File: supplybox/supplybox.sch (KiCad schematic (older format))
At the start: 12 parts, among them J1 Screw_Terminal_01x02

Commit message: v1.0
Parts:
- removed C?: CP, symbol Device:CP
- removed FL1: EMI_Filter_CommonMode, Inductor_THT:L_CommonMode_Wuerth_WE-CMB-XS, symbol Device:EMI_Filter_CommonMode
- removed J1: Screw_Terminal_01x02, symbol Connector:Screw_Terminal_01x02
- added C10, C6: 470uF, Capacitor_THT:CP_Radial_D8.0mm_P3.50mm, symbol Device:CP
- added C11, C4, C7, C8: 100uF, Capacitor_THT:CP_Radial_D6.3mm_P2.50mm, symbol Device:CP
- added C2: 100nF, Capacitor_SMD:C_0603_1608Metric_Pad1.05x0.95mm_HandSolder, symbol Device:C
- added C5, C9: 470pF, Capacitor_SMD:C_0603_1608Metric_Pad1.05x0.95mm_HandSolder, symbol Device:C
- added D4, D5: 1N5819, Diode_THT:D_DO-41_SOD81_P10.16mm_Horizontal, symbol Diode:1N5819
- added FL1: L_Core_Ferrite_Coupled_1243, Inductor_THT:L_CommonMode_Wuerth_WE-CMB-XS, symbol Device:L_Core_Ferrite_Coupled_1243
- added H1, H2, H3, H4, H5, H6, H7, H8: MountingHole_Pad, MountingHole:MountingHole_3.2mm_M3_DIN965_Pad, symbol Mechanical:MountingHole_Pad
- added L1, L3: 220 uH, Inductor_THT:L_Radial_D9.5mm_P5.00mm_Fastron_07HVP, symbol Device:L_Core_Ferrite
- added L2, L4: 1uH, Inductor_SMD:L_0805_2012Metric_Pad1.15x1.40mm_HandSolder, symbol Device:L_Core_Ferrite
- added R2, R5: 0.3 Ohm, Resistor_SMD:R_0805_2012Metric_Pad1.15x1.40mm_HandSolder, symbol Device:R
- added R3: 1200, Resistor_SMD:R_0603_1608Metric_Pad1.05x0.95mm_HandSolder, symbol Device:R
- added R4, R7: 3900, Resistor_SMD:R_0603_1608Metric_Pad1.05x0.95mm_HandSolder, symbol Device:R
- added R6: 2200, Resistor_SMD:R_0603_1608Metric_Pad1.05x0.95mm_HandSolder, symbol Device:R
- added RV1, RV2: 0-200, Potentiometer_SMD:Potentiometer_Bourns_TC33X_Vertical, symbol Device:R_POT_TRIM
- added TH1: Thermistor_NTC, Resistor_THT:R_Axial_DIN0204_L3.6mm_D1.6mm_P5.08mm_Horizontal, symbol Device:Thermistor_NTC
- added TP1, TP10, TP2, TP3, TP4, TP8, TP9: TestPoint, TestPoint:TestPoint_Pad_D1.0mm, symbol Connector:TestPoint
- added U1: EPM1210SJ_1212AE, ERIG_Converter_DCDC:EPMXX10SJ_XXXXAE, symbol ERIG_Converter_DCDC:EPM1210SJ_1212AE
- added U2, U3: MC33063AD, Package_SO:SOIC-8_3.9x4.9mm_P1.27mm, symbol Regulator_Switching:MC33063AD
- C1: value 1000uF -> 100uF; footprint (none) -> Capacitor_THT:CP_Radial_D18.0mm_P7.50mm; digikey (none) -> 565-1481-ND
- C3: renamed from C?; value C -> 47nF; footprint (none) -> Capacitor_SMD:C_0603_1608Metric_Pad1.05x0.95mm_HandSolder; digikey (none) -> 1292-1446-1-ND
- D1: renamed from D?; footprint (none) -> ERIG_Diode:KBP20XXG; digikey (none) -> KBP206GDI-ND
- D2: renamed from D?; value D_Zener 13V -> 13V; footprint (none) -> Diode_SMD:D_SOT-23_ANK; digikey (none) -> BZX84C13LT1GOSCT-ND
- D3: renamed from D?; footprint (none) -> Package_TO_SOT_THT:TO-92; digikey (none) -> 1740-1089-1-ND
- F1, F2: footprint (none) -> ERIG_Fuse:RST_XXX; digikey RST100AMMO-ND -> 507-1166-ND
- F3: footprint (none) -> Fuse:Fuse_0805_2012Metric_Pad1.15x1.40mm_HandSolder; digikey (none) -> MFU08051.00CT-ND
- R1: renamed from R?; value R -> 1K; footprint (none) -> Resistor_SMD:R_0603_1608Metric_Pad1.05x0.95mm_HandSolder; digikey (none) -> RHM1.0KDCT-ND
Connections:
- net labels added: +12V, +3.3V, +5V, 12V_Unfused, DC+L, GND
- wire segments 38 -> 108
- no-connect marks 0 -> 2
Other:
- moved on the sheet: C1, C3, D1, D2, D3, F1, F2, F3, R1

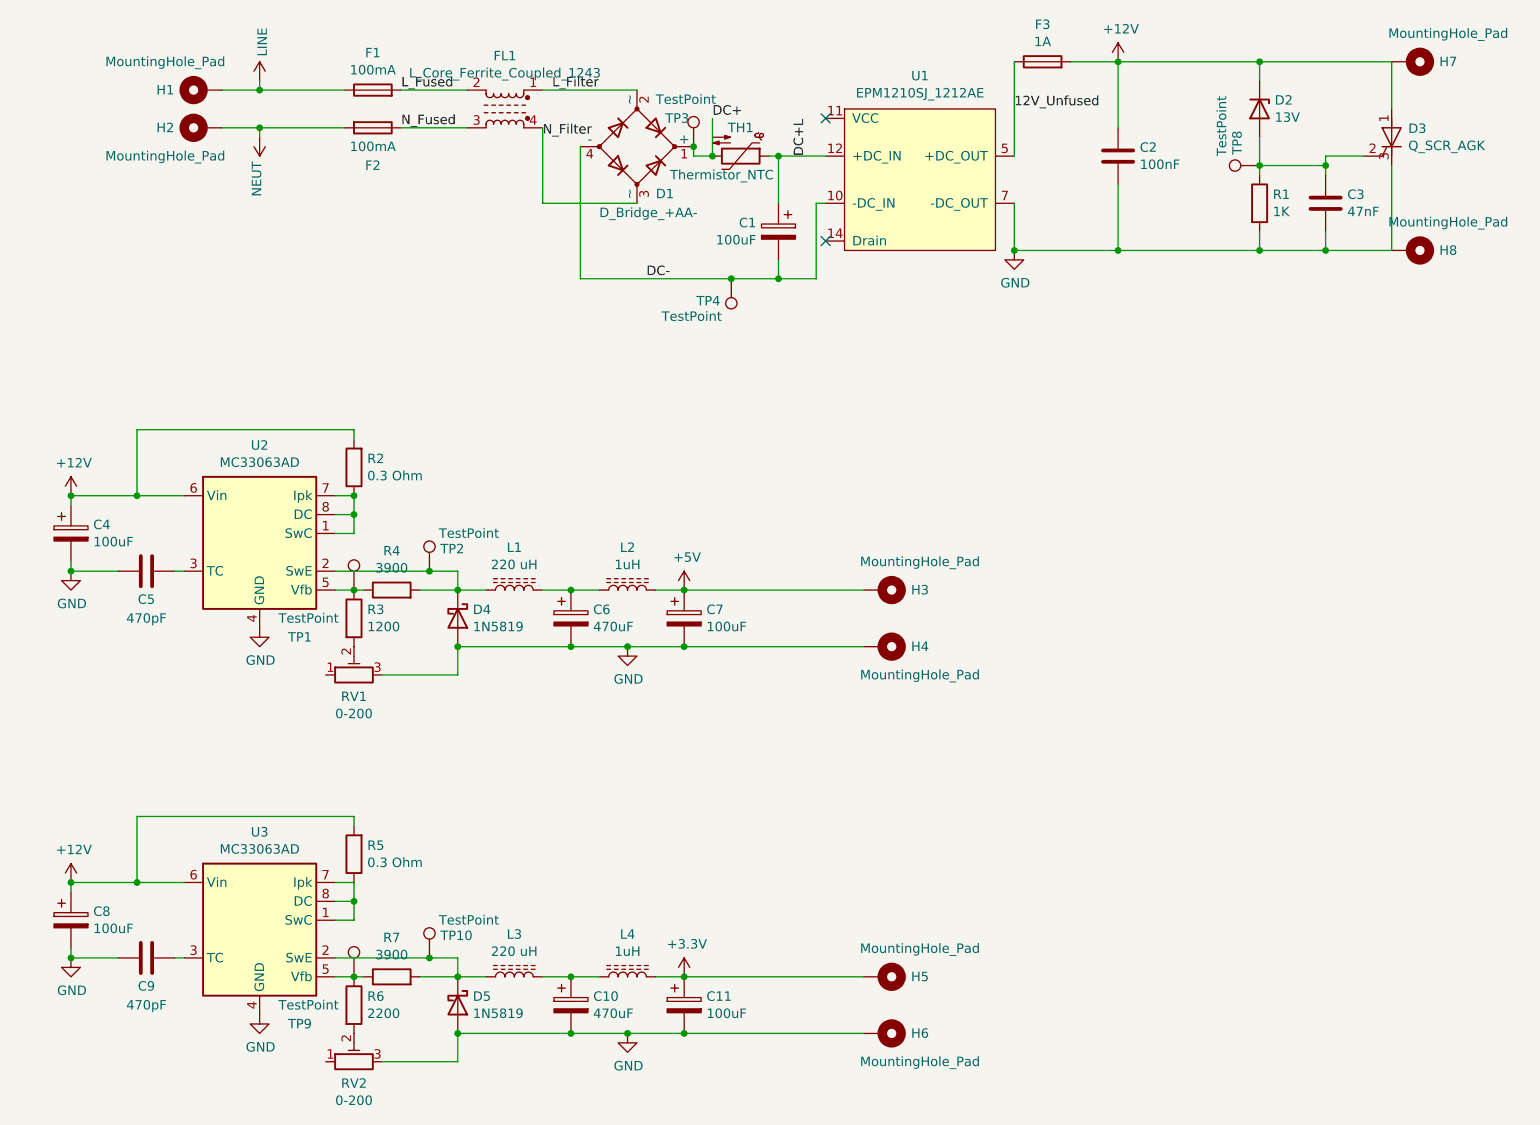
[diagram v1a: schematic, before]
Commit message: redo pcb and fix issues with schematic
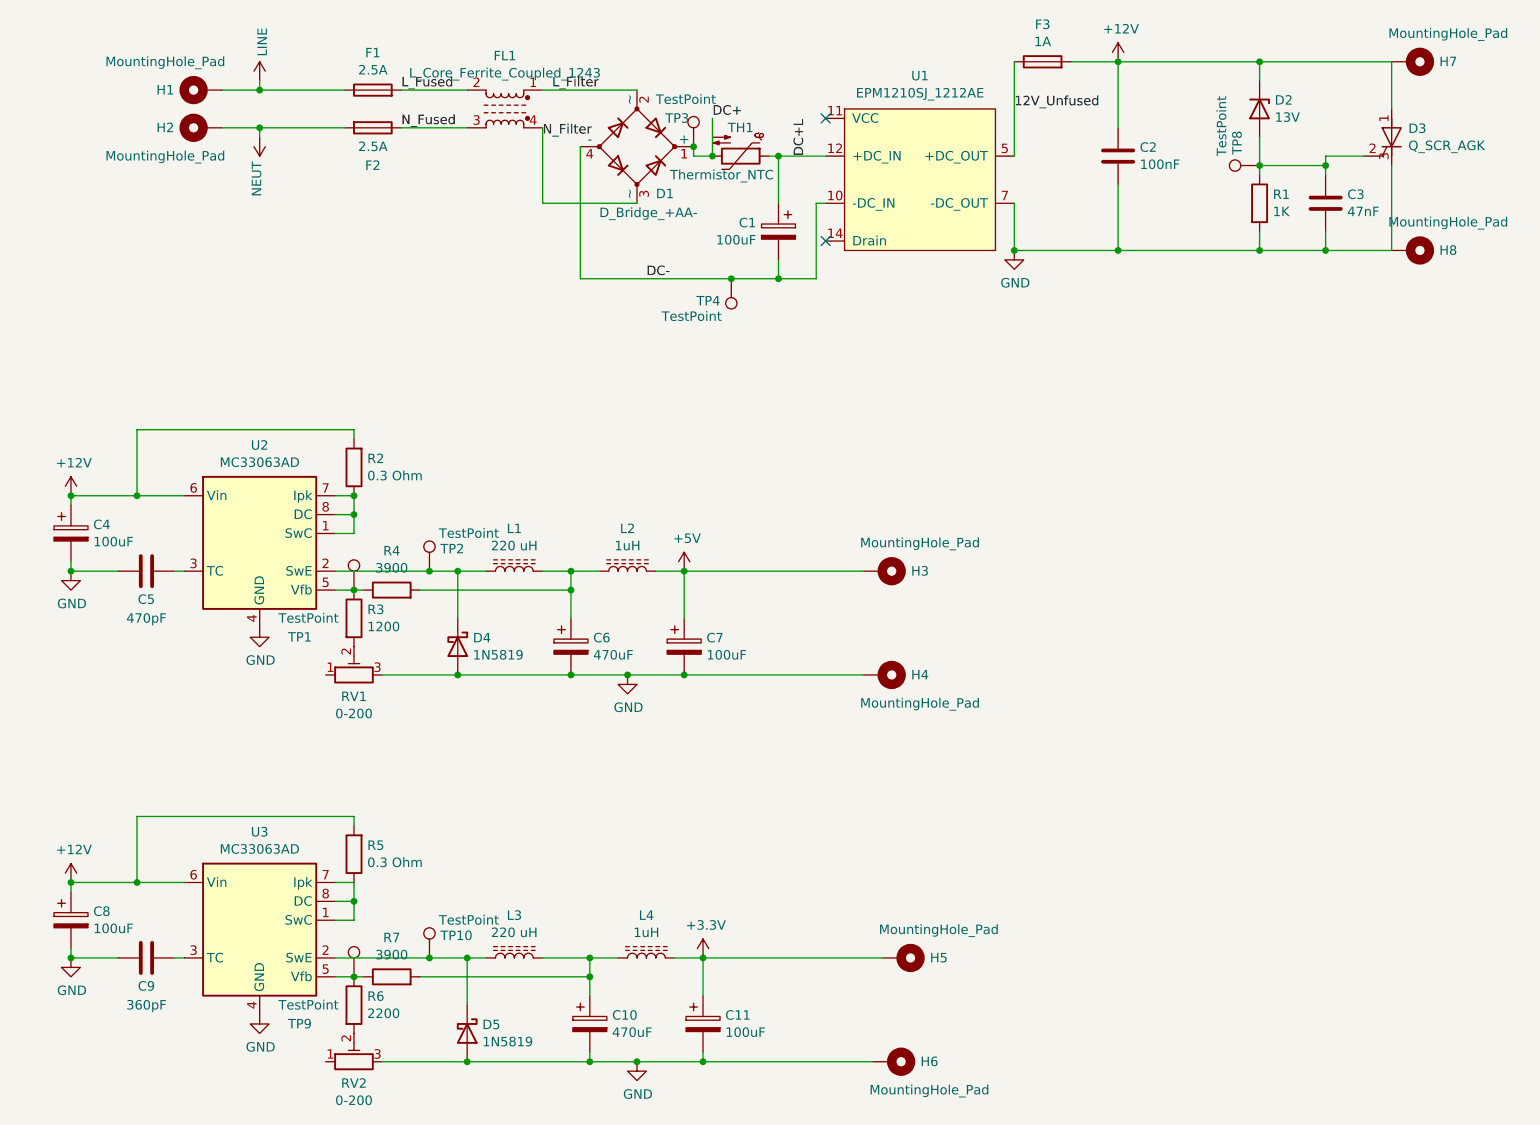
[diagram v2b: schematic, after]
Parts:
- C10, C6: footprint Capacitor_THT:CP_Radial_D8.0mm_P3.50mm -> Capacitor_SMD:CP_Elec_10x10.5; digikey 399-15679-ND -> PCE3805CT-ND
- C11, C4, C7, C8: footprint Capacitor_THT:CP_Radial_D6.3mm_P2.50mm -> Capacitor_SMD:C_Elec_6.3x7.7; digikey 732-8630-1-ND -> PCE3797CT-ND
- C2, C3, C5: footprint Capacitor_SMD:C_0603_1608Metric_Pad1.05x0.95mm_HandSolder -> Capacitor_SMD:C_0603_1608Metric_Pad1.08x0.95mm_HandSolder
- C9: value 470pF -> 360pF; footprint Capacitor_SMD:C_0603_1608Metric_Pad1.05x0.95mm_HandSolder -> Capacitor_SMD:C_0603_1608Metric_Pad1.08x0.95mm_HandSolder; digikey 1292-1530-1-ND -> 478-10353-1-ND
- D3: footprint Package_TO_SOT_THT:TO-92 -> Package_TO_SOT_THT:TO-92_Inline_Wide
- D4, D5: footprint Diode_THT:D_DO-41_SOD81_P10.16mm_Horizontal -> Diode_SMD:D_SOD-123F; digikey 497-7053-1-ND -> NTS245SFT1GOSCT-ND
- F1, F2: value 100mA -> 2.5A; digikey 507-1166-ND -> 507-2365-1-ND
- R1, R3, R4, R6, R7: footprint Resistor_SMD:R_0603_1608Metric_Pad1.05x0.95mm_HandSolder -> Resistor_SMD:R_0603_1608Metric_Pad0.98x0.95mm_HandSolder
- R2, R5: footprint Resistor_SMD:R_0805_2012Metric_Pad1.15x1.40mm_HandSolder -> Resistor_SMD:R_0805_2012Metric_Pad1.20x1.40mm_HandSolder; digikey YAG1861CT-ND -> RL12S.30FDKR-ND‎
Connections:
- net at D4.1 (K), L1.1, TP2.1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: no longer R4.2
- net at C6.1, L1.2, L2.1: now also R4.2
- net at D5.1 (K), L3.1, TP10.1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: no longer R7.2
- net at C10.1, L3.2, L4.1: now also R7.2
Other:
- moved on the sheet: C10, C11, C6, C7, D4, D5, H3, H4, H5, H6, L2, L3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
